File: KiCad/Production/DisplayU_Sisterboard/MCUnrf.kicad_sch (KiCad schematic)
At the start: 3 parts

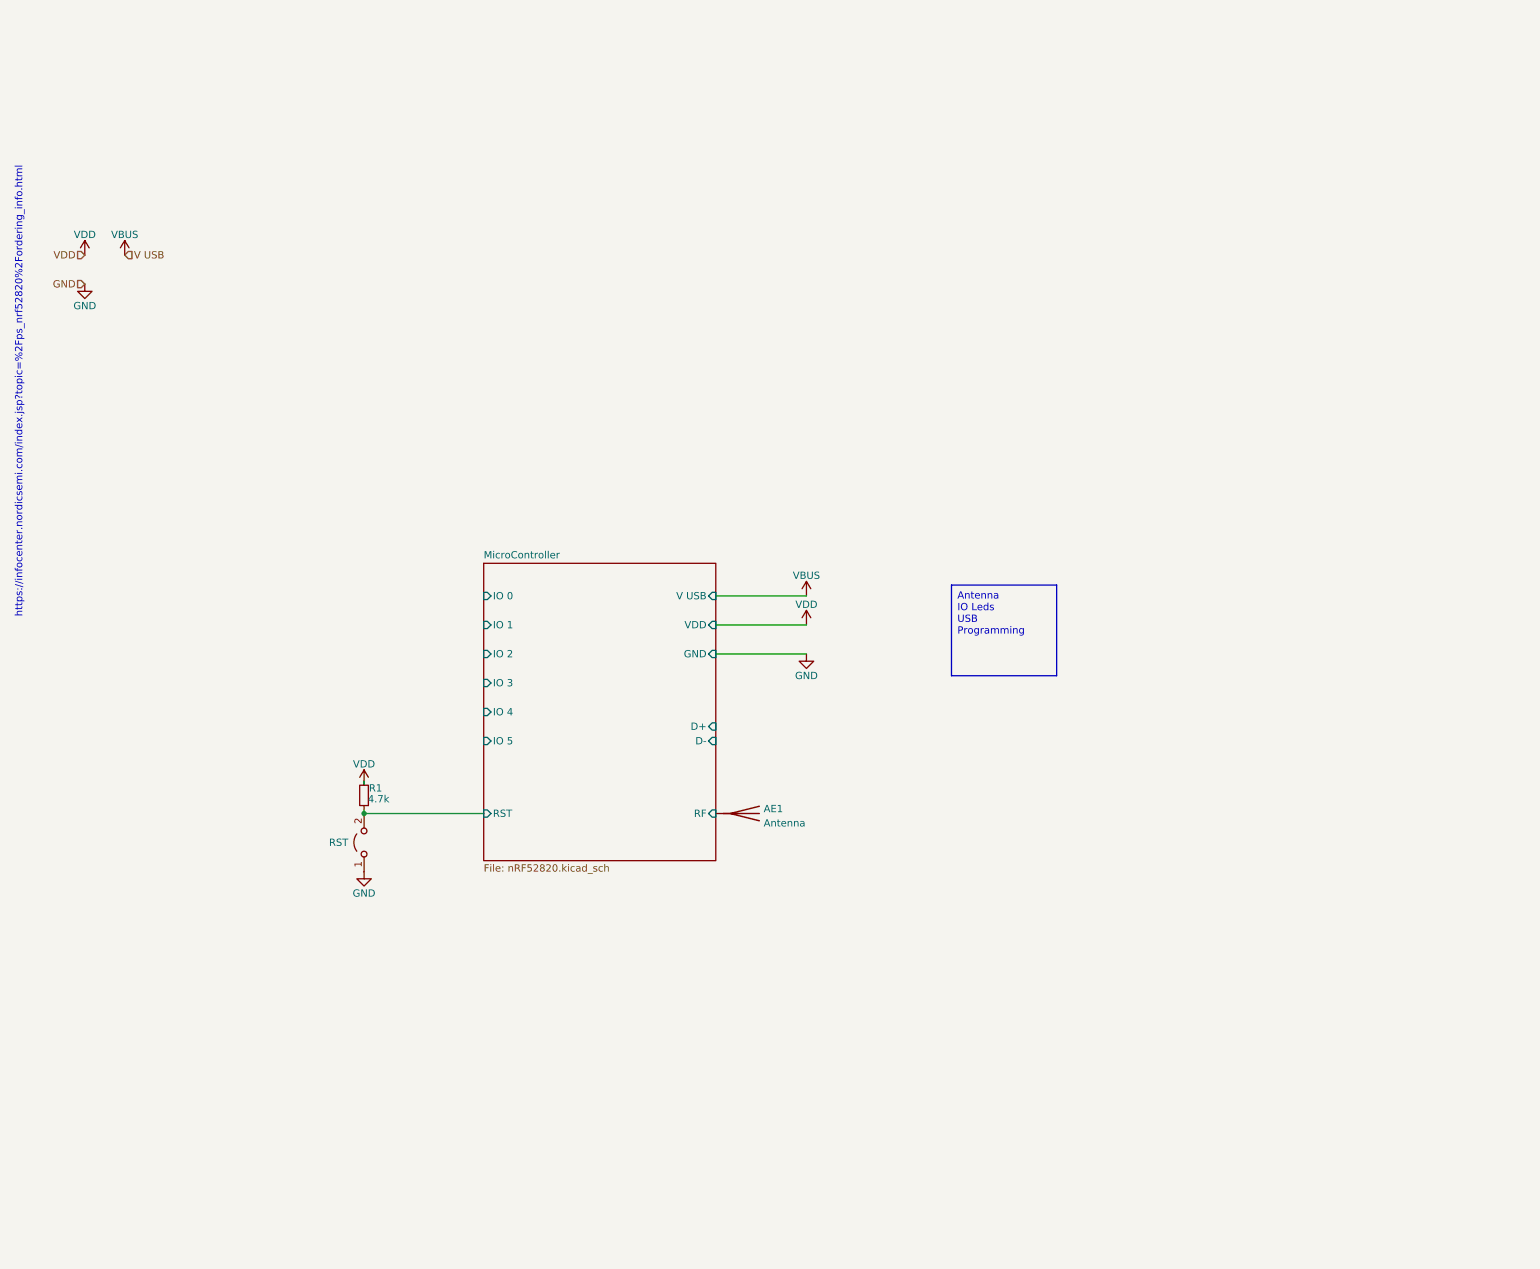
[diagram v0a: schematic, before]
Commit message: Display U is like 99% finished
- BMS Chips prob not needed
- LDO Chip prob not needed
- Final touches
> Start on routing
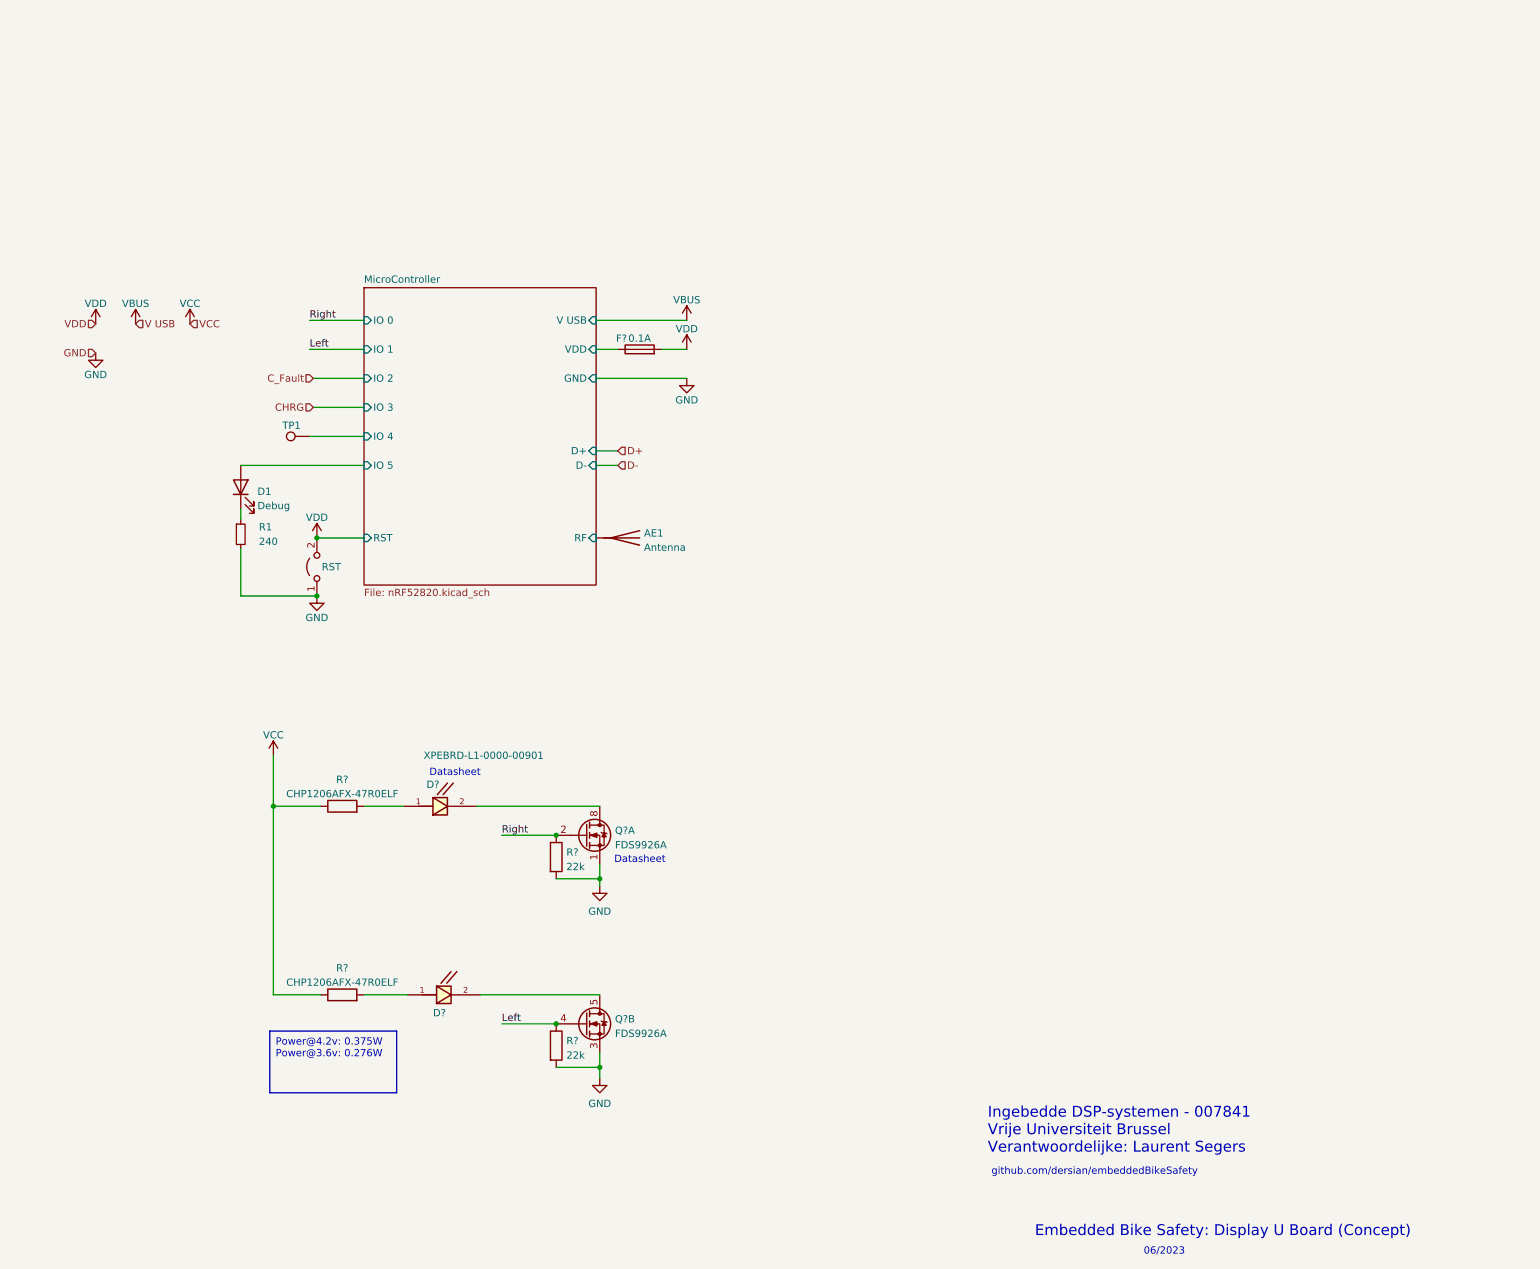
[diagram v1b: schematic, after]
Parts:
- added D1: Debug, Diode_SMD:D_0603_1608Metric, symbol Device:LED
- added D? (x2): XPEBRD-L1-0000-00901, XPEBRD-L1-0000-00901:LED_XPEBRD-L1-0000-00901, symbol XPEBRD-L1-0000-00901:XPEBRD-L1-0000-00901
- added F?: 0.1A, symbol Device:Fuse
- added Q? (x2): FDS9926A, Package_SO:SOIC-8_3.9x4.9mm_P1.27mm, symbol Transistor_FET:FDS9926A
- added R? (x2): CHP1206AFX-47R0ELF, Resistor_SMD:R_0603_1608Metric, symbol Device:R
- added R? (x2): 22k, Resistor_SMD:R_0603_1608Metric, symbol Device:R
- added TP1: TestPoint, symbol Connector:TestPoint
- AE1: footprint (none) -> RF_Antenna:Texas_SWRA117D_2.4GHz_Left
- R1: value 4.7k -> 240
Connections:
- net GND: now also R1.2, Q?.1 (S1), Q?.3 (S2), R?.2, R?.2
- net MicroController/IO 4: now also TP1.1
- net MicroController/IO 5: now also D1.2 (A)
- net VDD: now also RST.2 (B), F?.2; no longer R1.2
- net MicroController/RST: no longer names the net of R1.1
- net MicroController/RST: now also D1.1 (K); no longer RST.2 (B)
- new net: D?.1, R?.2 (x2)
- new net: D?.2, Q?.7 (D1), Q?.8 (D1)
- new net: D?.2, Q?.5 (D2), Q?.6 (D2)
- new net Left: Q?.4 (G2), R?.1
- new net MicroController/VDD: F?.1
- new net Right: Q?.2 (G1), R?.1
- new net VCC: R?.1, R?.1
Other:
- note added: "06/2023"
- note added: "Datasheet"
- note added: "Embedded Bike Safety: Display U Board (Concept)"
- note added: "Ingebedde DSP-systemen - 007841 Vrije Universiteit Brussel Verantwoordelijke: Laurent Segers"
- note added: "github.com/dersian/embeddedBikeSafety"
- note removed: "https://infocenter.nordicsemi.com/index.jsp?topic=%2Fps_nrf52820%2Fordering_info.html"
- moved on the sheet: AE1, RST

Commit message: Schematic is done
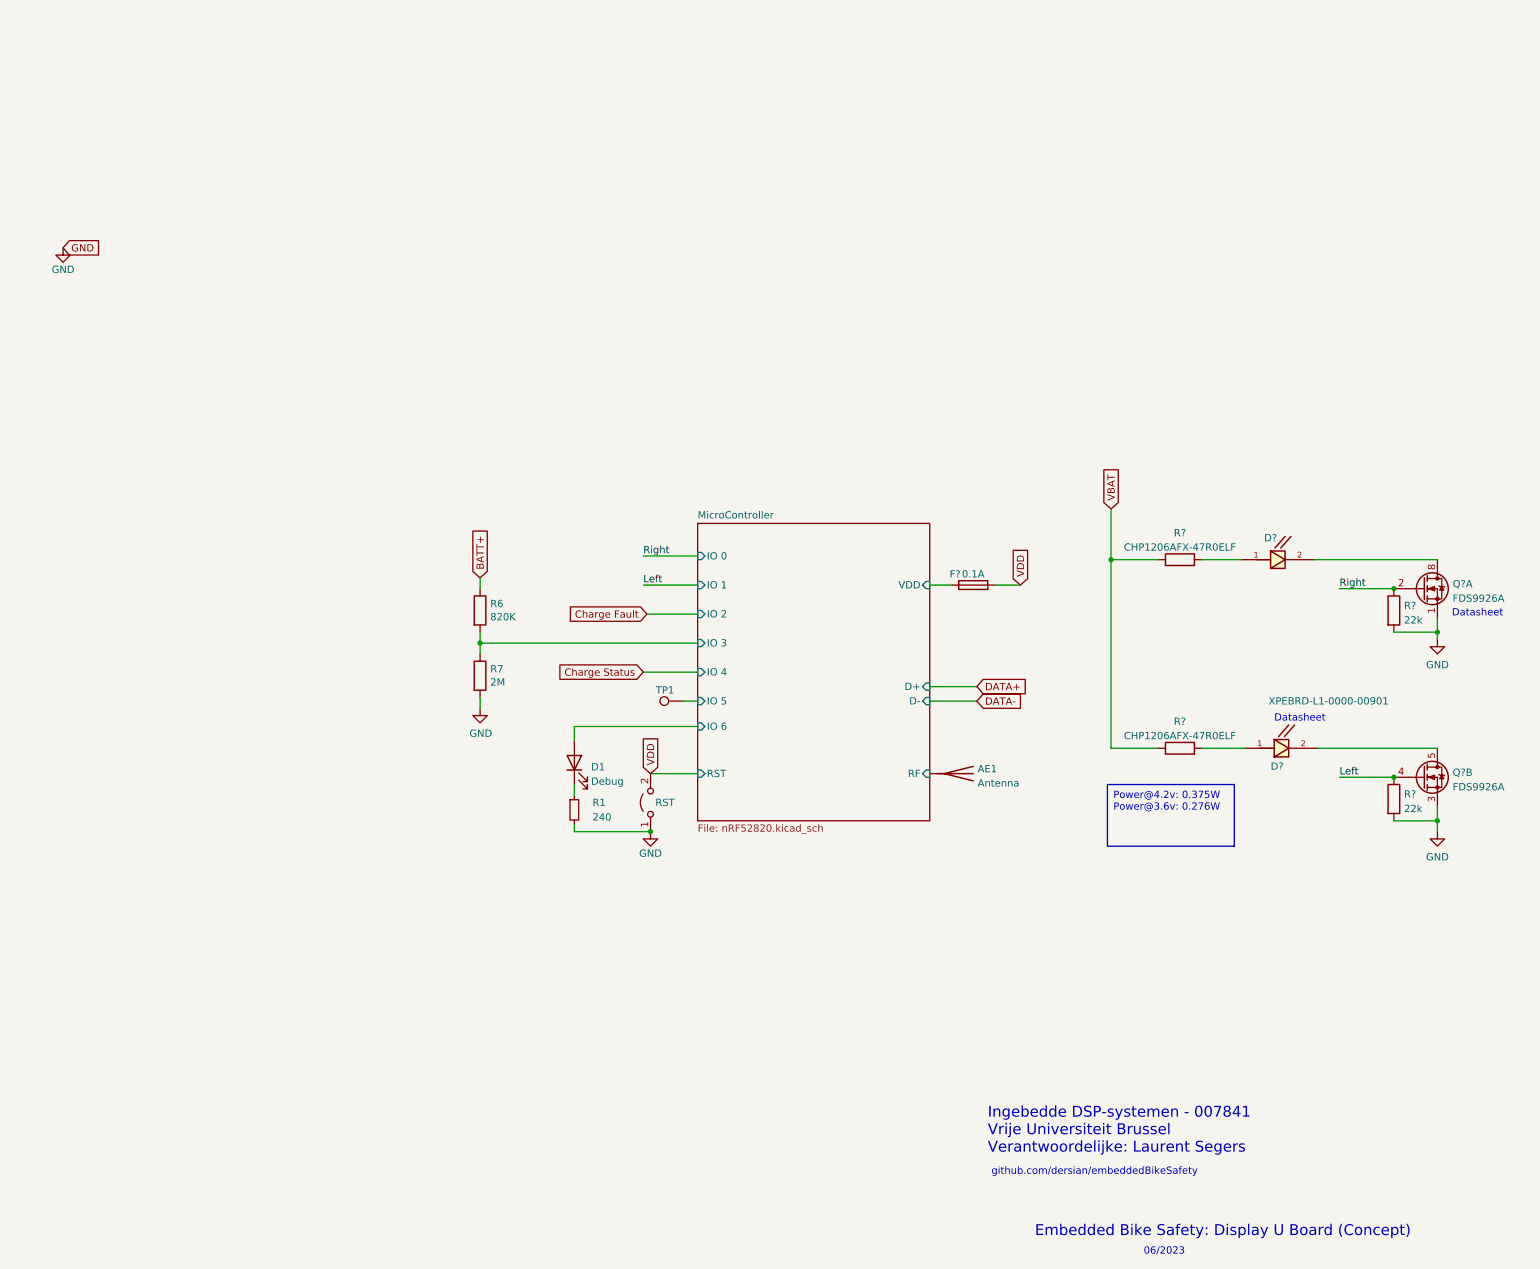
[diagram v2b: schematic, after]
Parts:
- added R6: 820K, Resistor_SMD:R_0603_1608Metric, symbol Device:R
- added R7: 2M, Resistor_SMD:R_0603_1608Metric, symbol Device:R
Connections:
- net MicroController/IO 4 is gone; now on net MicroController/IO 5: TP1.1
- net GND: now also R7.2
- net MicroController/IO 5: no longer D1.2 (A)
- net VCC renamed VBAT
- new net BATT+: R6.1
- new net MicroController/IO 3: R6.2, R7.1
- new net MicroController/IO 6: D1.2 (A)
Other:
- sheet MicroController ports: added IO 6; removed GND, V USB
- moved on the sheet: AE1, D1, D?, F?, Q?A, Q?B, R1, R?, RST

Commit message: Routing
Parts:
- removed D1: Debug, Diode_SMD:D_0603_1608Metric, symbol Device:LED
- removed F?: 0.1A, symbol Device:Fuse
- removed R1: 240, symbol Device:R_Small
- D? (x2): footprint XPEBRD-L1-0000-00901:LED_XPEBRD-L1-0000-00901 -> VUBRacing_ELO:XPEBRD-L1-0000-00901
- RST: footprint (none) -> Button_Switch_SMD:SW_SPST_B3U-1000P
- TP1: footprint (none) -> TestPoint:TestPoint_Pad_D2.0mm
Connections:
- net VDD: no longer RST.2 (B)
- new net MicroController/RST: RST.2 (B)
- no-connect marks 0 -> 1
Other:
- note added: "- Sam Dilmaghanian"

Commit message: Berekening/Metingen Verslag
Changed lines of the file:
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@@
   (symbol (lib_id "Transistor_FET:FDS9926A") (at 254 77.47 0) (unit 1)
     (in_bom yes) (on_board yes) (dnp no) (fields_autoplaced)
-    (property "Reference" "Q?" (at 259.207 76.6353 0)
+    (property "Reference" "Q?" (at 259.207 76.6452 0)
       (effects (font (size 1.27 1.27)) (justify left))
     )
-    (property "Value" "FDS9926A" (at 259.207 79.1722 0)
+    (property "Value" "FDS9926A" (at 259.207 79.1504 0)
       (effects (font (size 1.27 1.27)) (justify left))
     )
